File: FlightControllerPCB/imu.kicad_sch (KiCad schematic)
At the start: 0 parts

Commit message: IMU circuit
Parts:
- added C2, C3, C4, C5: 1uF, symbol Device:C
- added Q1: BSS138, Package_TO_SOT_SMD:SOT-23, symbol Transistor_FET:BSS138
- added R2, R3, R4, R5, R6: 2.2k, symbol Device:R
- added U1: (no value), symbol ICM_20948_custom:ICM_20948
- added U2: AP2112K-1.8, Package_TO_SOT_SMD:SOT-23-5, symbol Regulator_Linear:AP2112K-1.8
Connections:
- new net: C2.1, U1.10 (REGOUT)
- new net: Q1.2 (S), R2.2
- new net: Q1.3 (D), R3.2
- new net +1.8V: C3.1, C4.1, Q1.1 (G), R2.1, R4.2, R5.2, R6.2, U1.13 (VDD), U1.8 (VDDIO), U2.5 (VOUT)
- new net FSYNC: R6.1, U1.11 (FSYNC)
- new net GND: C2.2, C3.2, C4.2, C5.2, U1.18 (GND), U1.19 (RESV), U1.20 (RESV), U2.2 (GND)
- new net IMU_AD0: R4.1, U1.9 (SDO/AD0)
- new net IMU_AUX_CL: U1.7 (AUX_CL)
- new net IMU_AUX_DA: U1.21 (AUX_DA)
- new net IMU_SCL: U1.23 (SCL/SCLK)
- new net IMU_SDA: U1.24 (SDA/SDI)
- new net INT: R5.1, U1.12 (INT1)
- new net VIN: C5.1, R3.1, U2.1 (VIN), U2.3 (EN)
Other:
- note added: "Check RESV Check Interrupt Level Shifting MOSFET circuit"

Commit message: Hella sheets
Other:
- moved on the sheet: Q1, R2, R3
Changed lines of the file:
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@@
 	)
 	(junction
-		(at 124.46 142.24)
+		(at 111.76 133.35)
 		(diameter 0)
 		(color 0 0 0 0)
@@
 	(wire
 		(pts
-			(xy 132.08 142.24) (xy 124.46 142.24)
+			(xy 119.38 133.35) (xy 111.76 133.35)
 		)
 		(stroke
@@
 	(wire
 		(pts
-			(xy 132.08 144.78) (xy 132.08 142.24)
+			(xy 119.38 135.89) (xy 119.38 133.35)
 		)
 		(stroke
@@
 	(wire
 		(pts
-			(xy 124.46 142.24) (xy 124.46 144.78)
+			(xy 111.76 133.35) (xy 111.76 135.89)
 		)
 		(stroke
@@
 	(wire
 		(pts
-			(xy 124.46 138.43) (xy 124.46 142.24)
-		)
-		(stroke
-			(width 0)
-			(type default)
-		)
-	)
-	(wire
-		(pts
-			(xy 137.16 152.4) (xy 140.97 152.4)
-		)
-		(stroke
-			(width 0)
-			(type default)
-		)
-	)
-	(wire
-		(pts
-			(xy 124.46 152.4) (xy 127 152.4)
+			(xy 111.76 129.54) (xy 111.76 133.35)
+		)
+		(stroke
+			(width 0)
+			(type default)
+		)
+	)
+	(wire
+		(pts
+			(xy 124.46 143.51) (xy 128.27 143.51)
+		)
+		(stroke
+			(width 0)
+			(type default)
+		)
+	)
+	(wire
+		(pts
+			(xy 111.76 143.51) (xy 114.3 143.51)
 		)
 		(stroke
@@
 	(symbol
 		(lib_id "power:+3.3V")
-		(at 140.97 144.78 0)
+		(at 128.27 135.89 0)
 		(unit 1)
 		(body_style 1)
@@
 		(fields_autoplaced yes)
 		(property "Reference" "#PWR014"
-			(at 140.97 148.59 0)
+			(at 128.27 139.7 0)
 			(hide yes)
 			(show_name no)
@@
 		)
 		(property "Value" "VIN"
-			(at 140.97 139.7 0)
+			(at 128.27 130.81 0)
 			(show_name no)
 			(do_not_autoplace no)
@@
 		)
 		(property "Footprint" ""
-			(at 140.97 144.78 0)
+			(at 128.27 135.89 0)
 			(hide yes)
 			(show_name no)
@@
 		)
 		(property "Datasheet" ""
-			(at 140.97 144.78 0)
+			(at 128.27 135.89 0)
 			(hide yes)
 			(show_name no)
@@
 		)
 		(property "Description" "Power symbol creates a global label with name \"+3.3V\""
-			(at 140.97 144.78 0)
+			(at 128.27 135.89 0)
 			(hide yes)
 			(show_name no)
@@
 	(symbol
 		(lib_id "Device:R")
-		(at 124.46 148.59 0)
+		(at 111.76 139.7 0)
 		(unit 1)
 		(body_style 1)
@@
 		(dnp no)
 		(property "Reference" "R2"
-			(at 127 147.3199 0)
+			(at 114.3 138.4299 0)
 			(show_name no)
 			(do_not_autoplace no)
@@
 		)
 		(property "Value" "2.2k"
-			(at 124.46 150.622 90)
+			(at 111.76 141.732 90)
 			(show_name no)
 			(do_not_autoplace no)
@@
 		)
 		(property "Footprint" ""
-			(at 122.682 148.59 90)
+			(at 109.982 139.7 90)
 			(hide yes)
 			(show_name no)
@@
 		)
 		(property "Datasheet" ""
-			(at 124.46 148.59 0)
+			(at 111.76 139.7 0)
 			(hide yes)
 			(show_name no)
@@
 		)
 		(property "Description" "Resistor"
-			(at 124.46 148.59 0)
+			(at 111.76 139.7 0)
 			(hide yes)
 			(show_name no)
@@
 	(symbol
 		(lib_id "Device:R")
-		(at 140.97 148.59 0)
+		(at 128.27 139.7 0)
 		(unit 1)
 		(body_style 1)
@@
 		(dnp no)
 		(property "Reference" "R3"
-			(at 143.51 147.3199 0)
+			(at 130.81 138.4299 0)
 			(show_name no)
 			(do_not_autoplace no)
@@
 		)
 		(property "Value" "2.2k"
-			(at 140.97 150.622 90)
+			(at 128.27 141.732 90)
 			(show_name no)
 			(do_not_autoplace no)
@@
 		)
 		(property "Footprint" ""
-			(at 139.192 148.59 90)
+			(at 126.492 139.7 90)
 			(hide yes)
 			(show_name no)
@@
 		)
 		(property "Datasheet" ""
-			(at 140.97 148.59 0)
+			(at 128.27 139.7 0)
 			(hide yes)
 			(show_name no)
@@
 		)
 		(property "Description" "Resistor"
-			(at 140.97 148.59 0)
+			(at 128.27 139.7 0)
 			(hide yes)
 			(show_name no)
@@
 	(symbol
 		(lib_id "Transistor_FET:BSS138")
-		(at 132.08 149.86 270)
+		(at 119.38 140.97 270)
 		(unit 1)
 		(body_style 1)
@@
 		(dnp no)
 		(property "Reference" "Q1"
-			(at 132.842 154.432 0)
+			(at 120.142 145.542 0)
 			(show_name no)
 			(do_not_autoplace no)
@@
 		)
 		(property "Value" "BSS138"
-			(at 121.666 155.956 90)
+			(at 108.966 147.066 90)
 			(show_name no)
 			(do_not_autoplace no)
@@
 		)
 		(property "Footprint" "Package_TO_SOT_SMD:SOT-23"
-			(at 130.175 154.94 0)
+			(at 117.475 146.05 0)
 			(hide yes)
 			(show_name no)
@@
 		)
 		(property "Datasheet" "https://www.onsemi.com/pub/Collateral/BSS138-D.PDF"
-			(at 128.27 154.94 0)
+			(at 115.57 146.05 0)
 			(hide yes)
 			(show_name no)
@@
 		)
 		(property "Description" "50V Vds, 0.22A Id, N-Channel MOSFET, SOT-23"
-			(at 132.08 149.86 0)
+			(at 119.38 140.97 0)
 			(hide yes)
 			(show_name no)
@@
 	(symbol
 		(lib_id "power:+3.3V")
-		(at 124.46 138.43 0)
+		(at 111.76 129.54 0)
 		(unit 1)
 		(body_style 1)
@@
 		(dnp no)
 		(property "Reference" "#PWR010"
-			(at 124.46 142.24 0)
+			(at 111.76 133.35 0)
 			(hide yes)
 			(show_name no)
@@
 		)
 		(property "Value" "+1.8V"
-			(at 121.412 134.112 0)
+			(at 108.712 125.222 0)
 			(show_name no)
 			(do_not_autoplace no)
@@
 		)
 		(property "Footprint" ""
-			(at 124.46 138.43 0)
+			(at 111.76 129.54 0)
 			(hide yes)
 			(show_name no)
@@
 		)
 		(property "Datasheet" ""
-			(at 124.46 138.43 0)
+			(at 111.76 129.54 0)
 			(hide yes)
 			(show_name no)
@@
 		)
 		(property "Description" "Power symbol creates a global label with name \"+3.3V\""
-			(at 124.46 138.43 0)
-			(hide yes)
-			(show_name no)
+			(at 111.76 129.54 0)
+			(hide yes)
+			(show_name no)

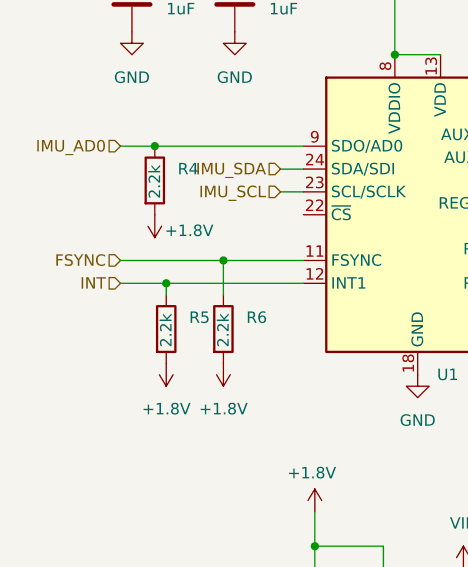
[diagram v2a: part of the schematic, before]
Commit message: initial baro/imu to mcu pins
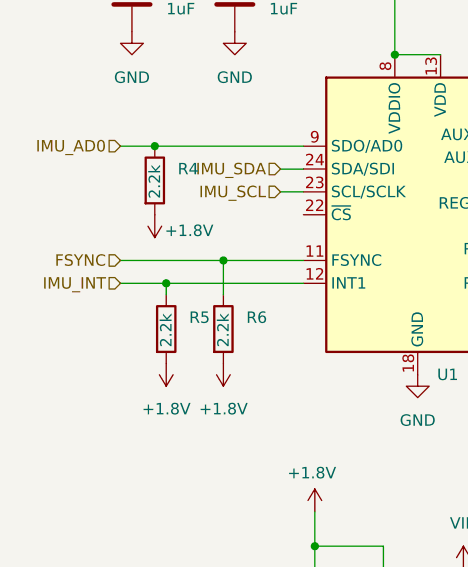
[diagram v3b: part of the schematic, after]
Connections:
- net INT renamed IMU_INT
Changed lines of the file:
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@@
 		)
 	)
-	(hierarchical_label "INT"
+	(hierarchical_label "IMU_INT"
 		(shape input)
 		(at 90.17 104.14 180)

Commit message: actually the IMU+baro changes
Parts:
- removed C5: 1uF, symbol Device:C
- removed U2: AP2112K-1.8, Package_TO_SOT_SMD:SOT-23-5, symbol Regulator_Linear:AP2112K-1.8

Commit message: Power circuit
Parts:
- removed Q1: BSS138, Package_TO_SOT_SMD:SOT-23, symbol Transistor_FET:BSS138
- removed R2, R3: 2.2k, symbol Device:R
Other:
- note added: "- MOSFET+Pull ups??? - quick AI circuit check - RESV check"
- note removed: "Check RESV Check Interrupt Level Shifting MOSFET circuit"

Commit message: early MCU setup
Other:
- note added: "- MOSFET+Pull ups??? - Sanity check - RESV check"
- note removed: "- MOSFET+Pull ups??? - quick AI circuit check - RESV check"
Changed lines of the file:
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@@
 	(generator_version "10.0")
 	(paper "A4")
-	(text "- MOSFET+Pull ups???\n- quick AI circuit check\n- RESV check"
+	(text "- MOSFET+Pull ups???\n- Sanity check\n- RESV check"
 		(exclude_from_sim no)
 		(at 181.61 65.024 0)

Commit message: Sanity check+Error fixes
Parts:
- added C23: .1uF, symbol Device:C
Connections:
- net +1.8V: now also C23.1
- net GND: now also C23.2
- net IMU_AUX_CL: no longer names the net of U1.7 (AUX_CL)
- net IMU_AUX_DA: no longer names the net of U1.21 (AUX_DA)
- no-connect marks 0 -> 3
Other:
- note removed: "- MOSFET+Pull ups??? - Sanity check - RESV check"
- moved on the sheet: C3, C4
